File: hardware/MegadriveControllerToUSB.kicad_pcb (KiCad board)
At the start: 2 copper layers, 32.5 x 44.2 mm, 13 parts, among them CON1 AVR-ISP6, J1 USB, J2 DB9, U1 ATMEGA32U2-AU, X1 16Mhz

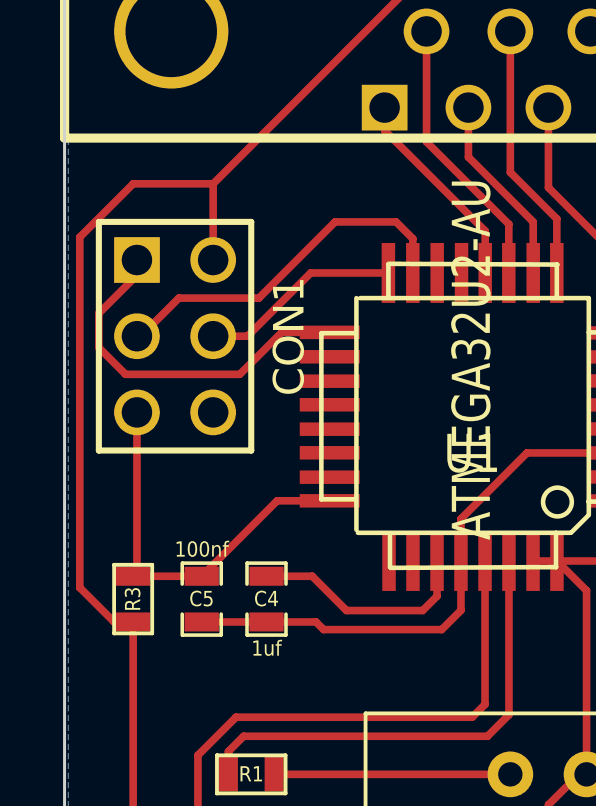
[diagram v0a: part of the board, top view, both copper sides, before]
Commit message: Set pin numbers properly. Need to test again. Removing some kicad temp files.
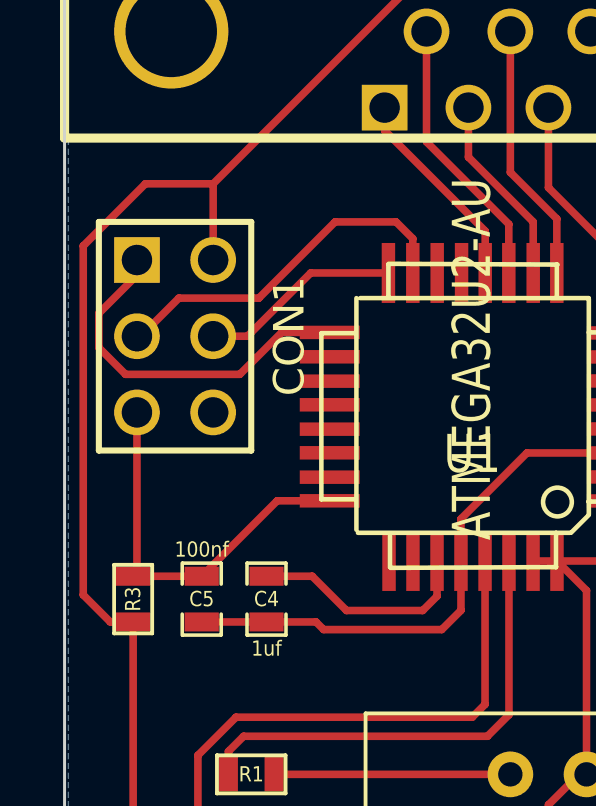
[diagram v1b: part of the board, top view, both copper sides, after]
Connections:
- net B_A_BUTTON renamed DATA5_PIN
- net C_START_BUTTON renamed DATA4_PIN
- net DOWN_Y renamed DATA1_PIN
- net LEFT_X renamed DATA2_PIN
- net RIGHT_MODE renamed DATA3_PIN
- net UP_Z renamed DATA0_PIN
